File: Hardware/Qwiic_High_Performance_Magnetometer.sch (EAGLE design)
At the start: 26 parts, among them J1 Qwiic, J2 Qwiic, U1 MMC5893MA_QFN16

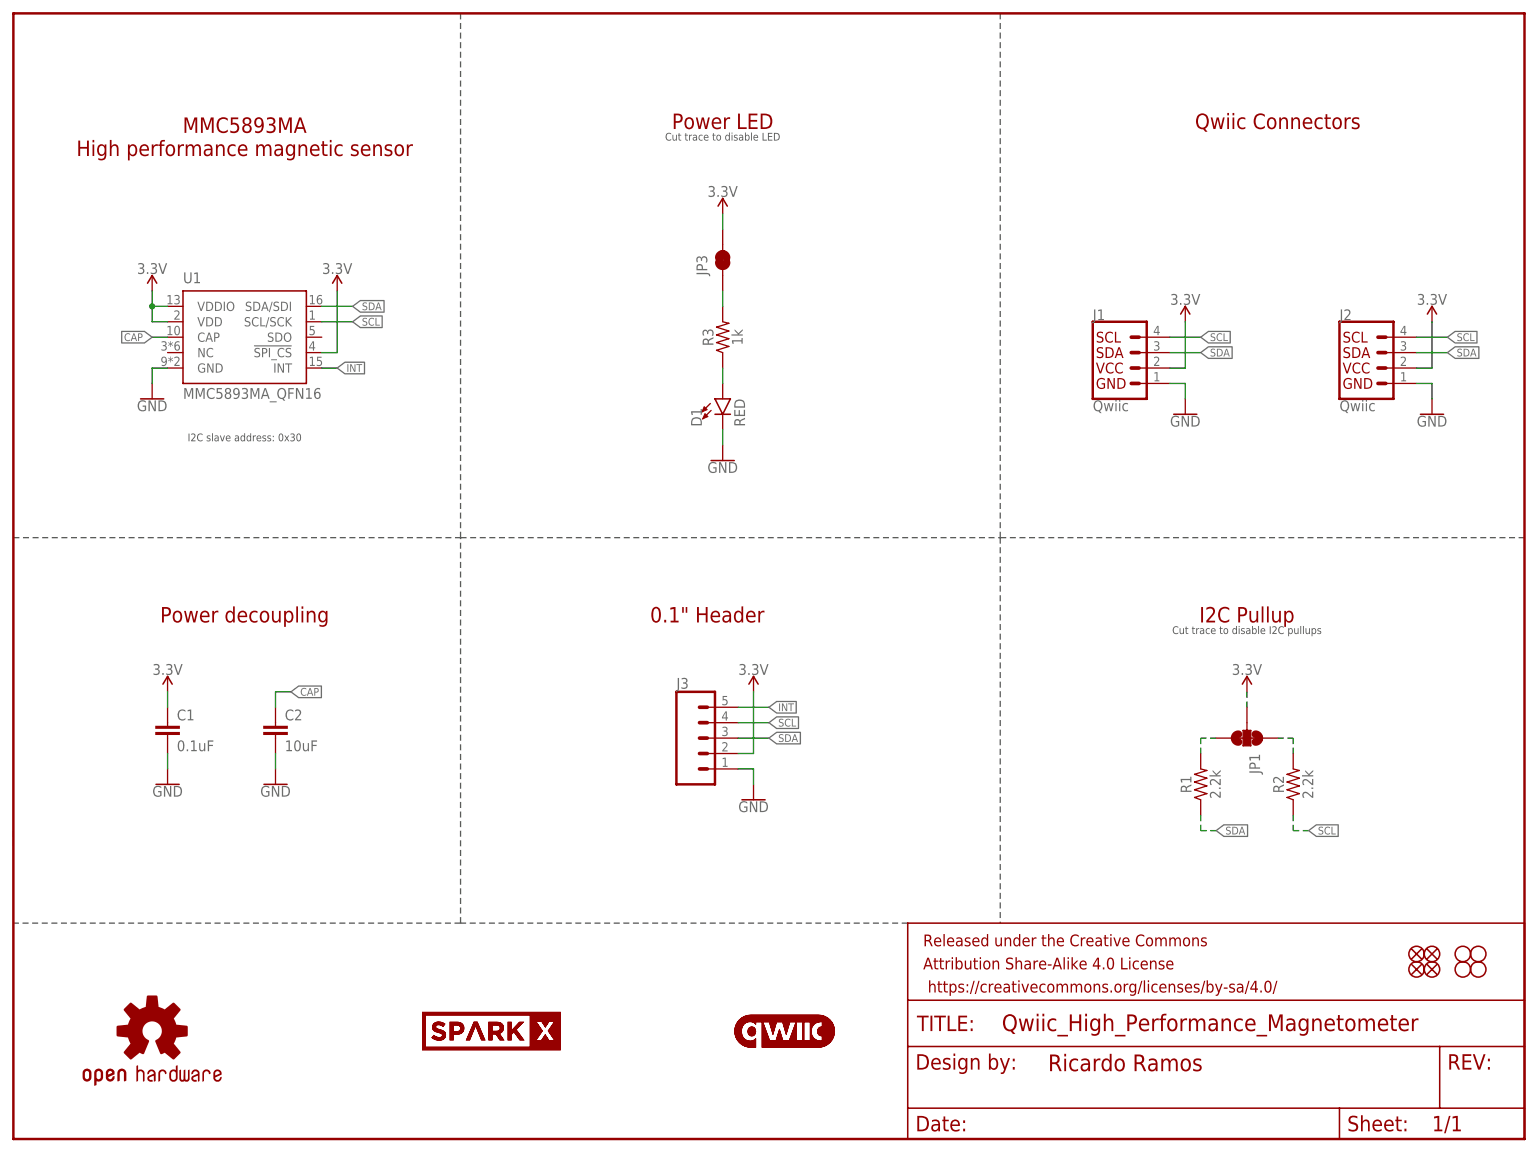
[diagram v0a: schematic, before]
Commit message: Added SPI breakout header; created PCB production files.
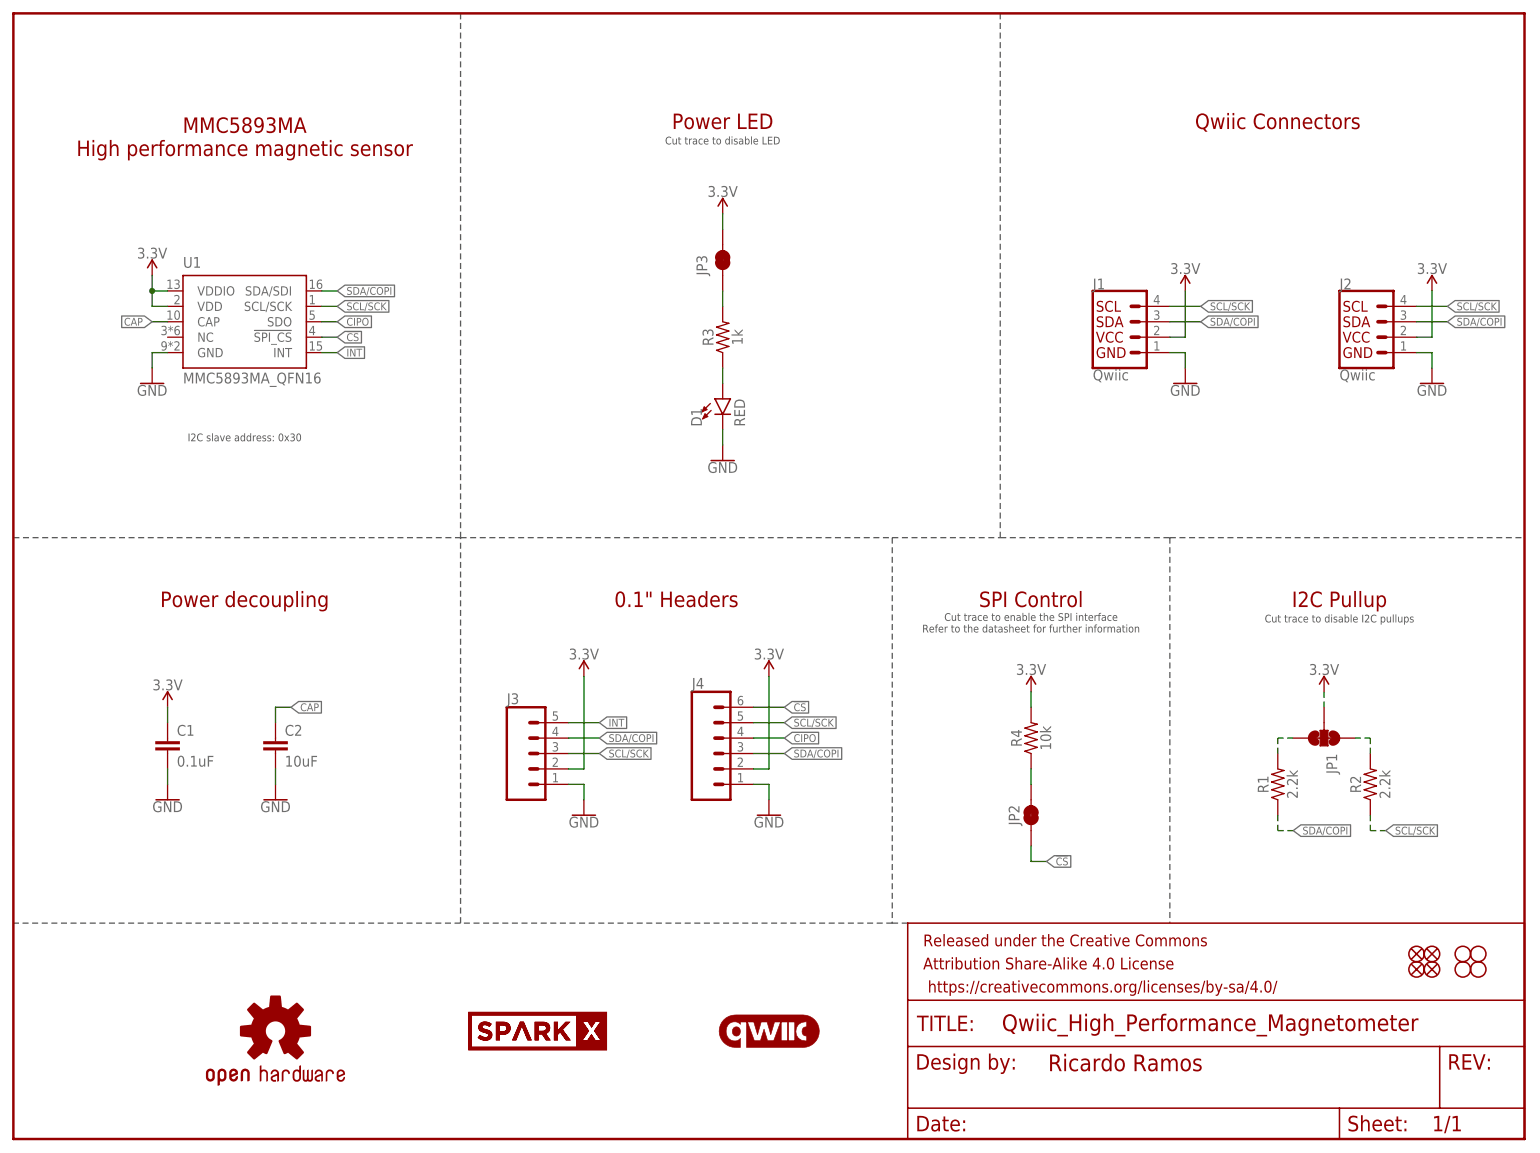
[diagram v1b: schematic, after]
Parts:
- removed LOGO3: QWIIC_LOGO_4MM, SparkFun-Aesthetics:QWIIC_LOGO_4MM
- removed U$1: SPARKX-LOGO5, SparkX:SPARKX-LOGO5
- removed U$2: SPARKX-LOGO3, SparkX:SPARKX-LOGO3
- added J4: (no value), SparkFun-Connectors:CONN_06NO_SILK_NO_POP
- added JP2: JUMPER-SMT_2_NC_TRACE_SILK, SparkFun-Jumpers:JUMPER-SMT_2_NC_TRACE_SILK
- added R4: 10k, SparkFun-Resistors:10KOHM-0603-1/10W-1%
- added U$36: SPARKX-LOGO2, SparkX:SPARKX-LOGO2
- added U$37: SPARKX-LOGO3, SparkX:SPARKX-LOGO3
- LOGO2: value QWIIC_LOGO_4MM -> QWIIC_LOGO_5MM; device SparkFun-Aesthetics:QWIIC_LOGO_4MM -> SparkFun-Aesthetics:QWIIC_LOGO_5MM
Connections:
- removed net SCL: J1.4, J2.4, J3.4, R2.1, U1.SCL/SCK
- removed net SDA: J1.3, J2.3, J3.3, R1.1, U1.SDA/SDI
- new net !CS!: J4.6, JP2.1, U1.!SPI_CS!
- new net CIPO: J4.4, U1.SDO
- new net N$5: JP2.2, R4.1
- new net SCL/SCK: J1.4, J2.4, J3.3, J4.5, R2.1, U1.SCL/SCK
- new net SDA/COPI: J1.3, J2.3, J3.4, J4.3, R1.1, U1.SDA/SDI
- net 3.3V: now also J4.2, R4.2; no longer U1.!SPI_CS!
- net GND: now also J4.1
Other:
- note added: "0.1" Headers"
- note added: "Cut trace to enable the SPI interface Refer to the datasheet for further information"
- note added: "SPI Control"
- note removed: "0.1" Header"
- moved on the sheet: C1, C2, J1, J2, J3, JP1, R1, R2, U1
